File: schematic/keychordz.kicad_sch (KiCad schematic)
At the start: 40 parts, among them IC1 MCP73833-BZI_UN, J1 USB_C_Receptacle_USB2.0, J2 Conn_01x04_Male, SW1 SW_Push, SW2 SW_Push, SW3 SW_Push, SW4 SW_Push, SW5 SW_Push, SW6 SW_Push, SW7 SW_Push, SW9 SW_SPST, U1 nRF52840_Breakout

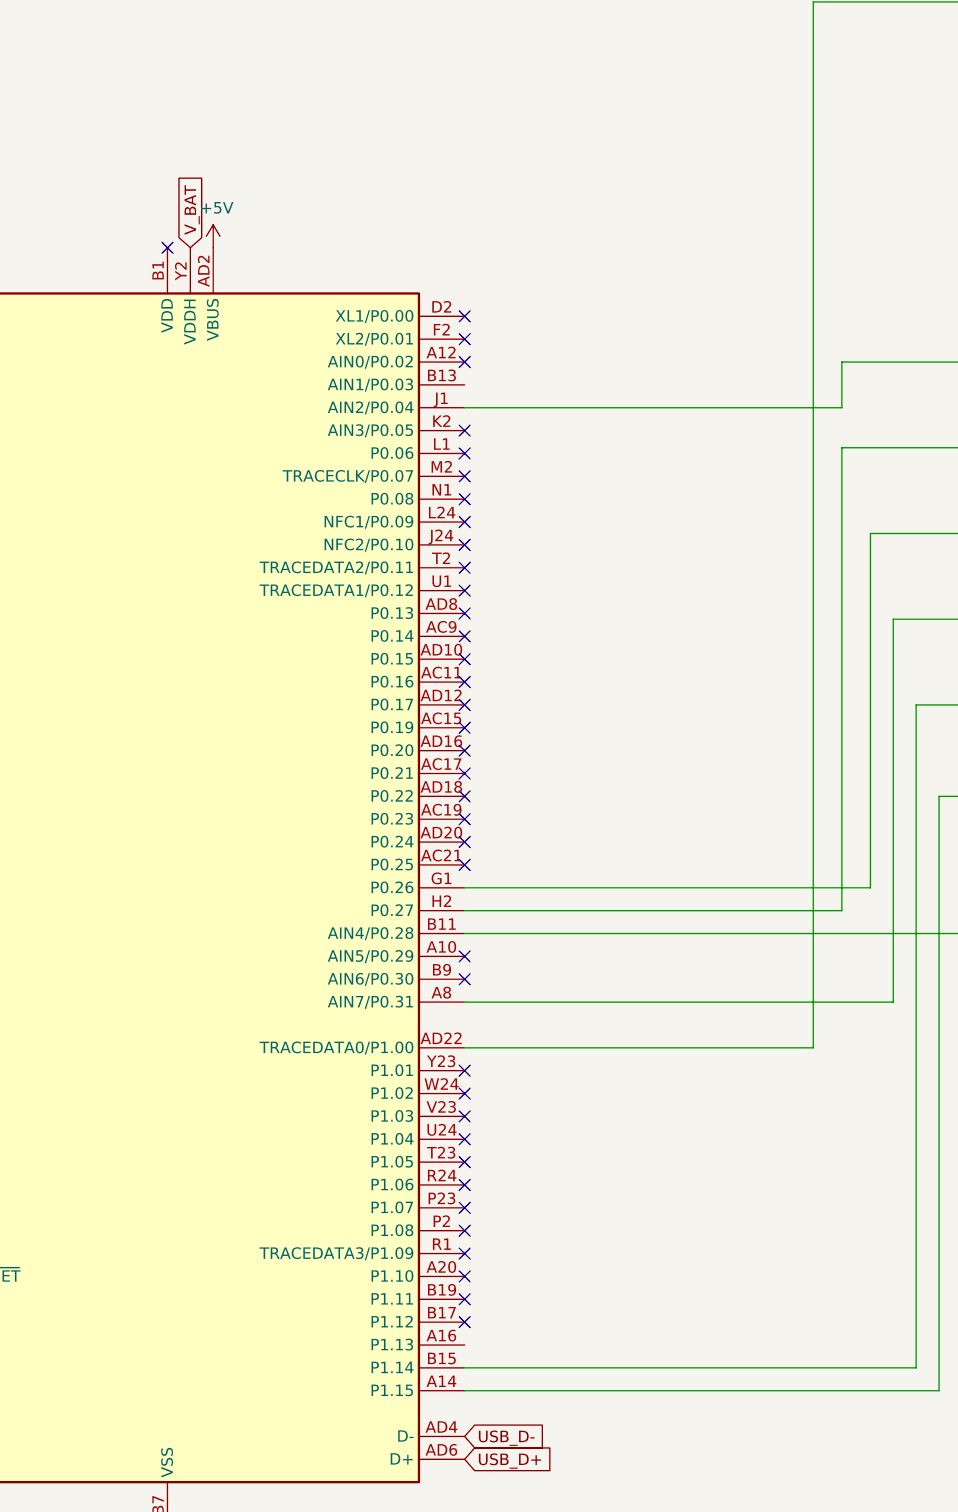
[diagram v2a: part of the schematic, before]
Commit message: update breakout without castellations
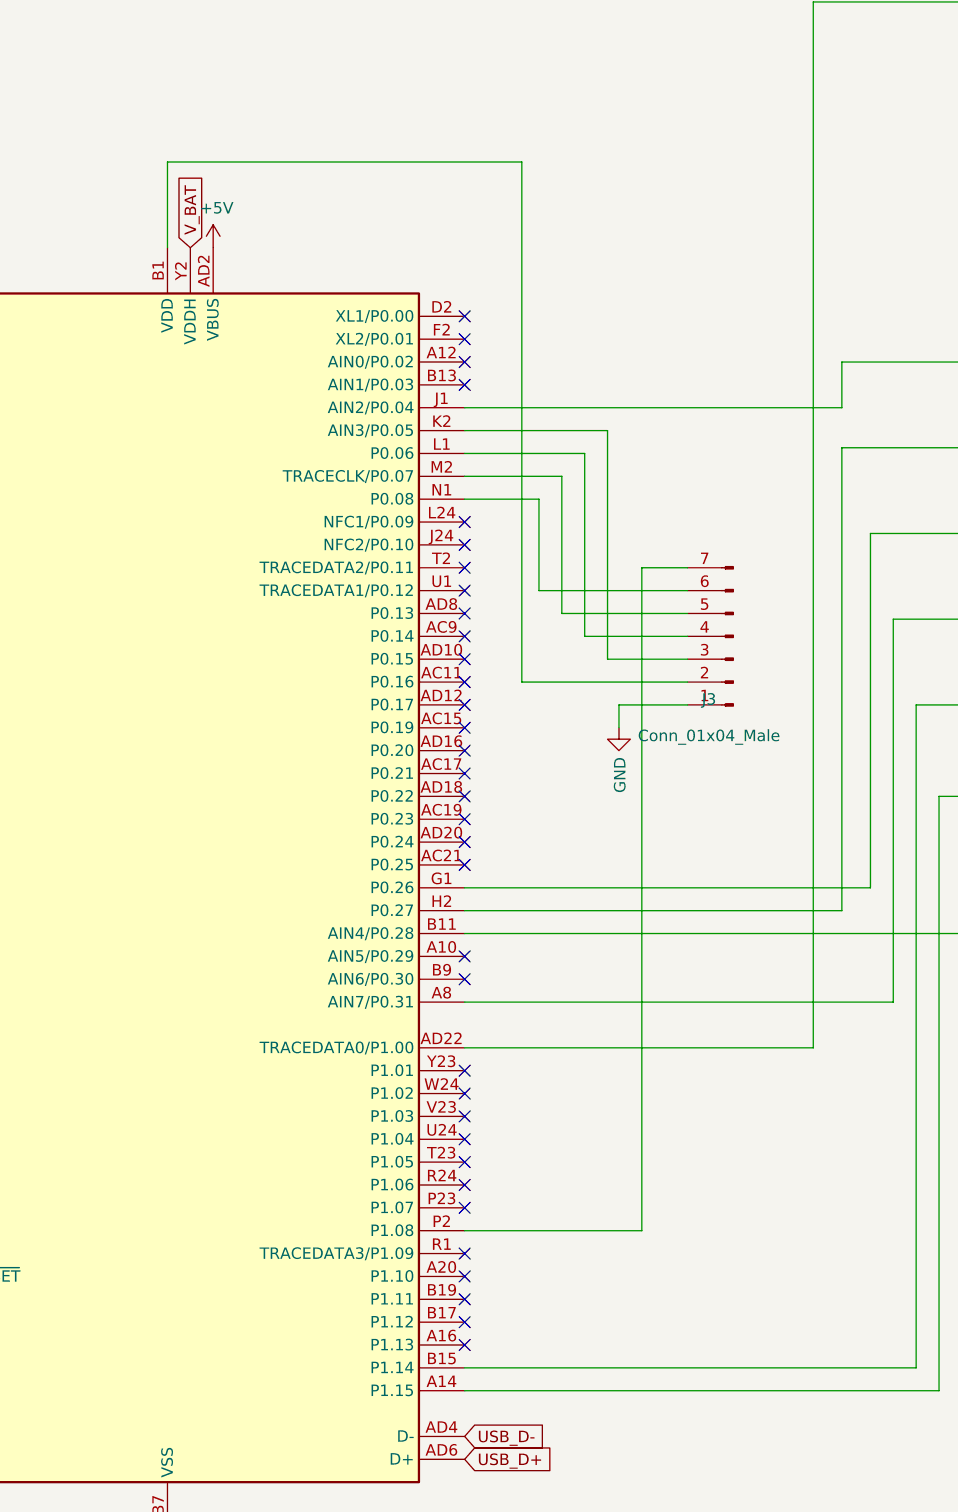
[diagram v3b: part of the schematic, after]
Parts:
- added J3: Conn_01x04_Male, Connector_PinHeader_2.54mm:PinHeader_1x07_P2.54mm_Vertical, symbol Connector:Conn_01x07_Male
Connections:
- net GND: now also J3.1 (Pin_1)
- net at U1.B1 (VDD): now also J3.2 (Pin_2)
- net at U1.K2 (AIN3/P0.05): now also J3.3 (Pin_3)
- net at U1.L1 (P0.06): now also J3.4 (Pin_4)
- net at U1.M2 (TRACECLK/P0.07): now also J3.5 (Pin_5)
- net at U1.N1 (P0.08): now also J3.6 (Pin_6)
- net at U1.P2 (P1.08): now also J3.7 (Pin_7)
- no-connect marks 41 -> 37
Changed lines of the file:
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@@
   (no_connect (at 46.355 53.34))
   (no_connect (at 46.355 55.88))
-  (no_connect (at 168.275 69.85))
   (no_connect (at 201.295 77.47))
   (no_connect (at 201.295 80.01))
   (no_connect (at 201.295 82.55))
-  (no_connect (at 201.295 90.17))
-  (no_connect (at 201.295 92.71))
-  (no_connect (at 201.295 95.25))
-  (no_connect (at 201.295 97.79))
+  (no_connect (at 201.295 85.09))
   (no_connect (at 201.295 100.33))
   (no_connect (at 201.295 102.87))
@@
   (no_connect (at 201.295 173.99))
   (no_connect (at 201.295 176.53))
-  (no_connect (at 201.295 179.07))
   (no_connect (at 201.295 181.61))
   (no_connect (at 201.295 184.15))
   (no_connect (at 201.295 186.69))
   (no_connect (at 201.295 189.23))
+  (no_connect (at 201.295 191.77))
   (wire (pts (xy 32.385 90.805) (xy 32.385 93.345))
     (stroke (width 0) (type solid) (color 0 0 0 0))
@@
     (stroke (width 0) (type solid) (color 0 0 0 0))
   )
+  (wire (pts (xy 168.275 60.325) (xy 207.645 60.325))
+    (stroke (width 0) (type solid) (color 0 0 0 0))
+  )
+  (wire (pts (xy 168.275 69.85) (xy 168.275 60.325))
+    (stroke (width 0) (type solid) (color 0 0 0 0))
+  )
   (wire (pts (xy 201.295 87.63) (xy 243.205 87.63))
     (stroke (width 0) (type solid) (color 0 0 0 0))
   )
+  (wire (pts (xy 201.295 90.17) (xy 217.17 90.17))
+    (stroke (width 0) (type solid) (color 0 0 0 0))
+  )
+  (wire (pts (xy 201.295 92.71) (xy 214.63 92.71))
+    (stroke (width 0) (type solid) (color 0 0 0 0))
+  )
+  (wire (pts (xy 201.295 95.25) (xy 212.09 95.25))
+    (stroke (width 0) (type solid) (color 0 0 0 0))
+  )
+  (wire (pts (xy 201.295 97.79) (xy 209.55 97.79))
+    (stroke (width 0) (type solid) (color 0 0 0 0))
+  )
   (wire (pts (xy 201.295 140.97) (xy 246.38 140.97))
     (stroke (width 0) (type solid) (color 0 0 0 0))
@@
     (stroke (width 0) (type solid) (color 0 0 0 0))
   )
+  (wire (pts (xy 201.295 179.07) (xy 220.98 179.07))
+    (stroke (width 0) (type solid) (color 0 0 0 0))
+  )
   (wire (pts (xy 201.295 194.31) (xy 251.46 194.31))
     (stroke (width 0) (type solid) (color 0 0 0 0))
   )
   (wire (pts (xy 201.295 196.85) (xy 254 196.85))
+    (stroke (width 0) (type solid) (color 0 0 0 0))
+  )
+  (wire (pts (xy 207.645 60.325) (xy 207.645 118.11))
+    (stroke (width 0) (type solid) (color 0 0 0 0))
+  )
+  (wire (pts (xy 207.645 118.11) (xy 226.06 118.11))
+    (stroke (width 0) (type solid) (color 0 0 0 0))
+  )
+  (wire (pts (xy 209.55 97.79) (xy 209.55 107.95))
+    (stroke (width 0) (type solid) (color 0 0 0 0))
+  )
+  (wire (pts (xy 209.55 107.95) (xy 226.06 107.95))
+    (stroke (width 0) (type solid) (color 0 0 0 0))
+  )
+  (wire (pts (xy 212.09 95.25) (xy 212.09 110.49))
+    (stroke (width 0) (type solid) (color 0 0 0 0))
+  )
+  (wire (pts (xy 212.09 110.49) (xy 226.06 110.49))
+    (stroke (width 0) (type solid) (color 0 0 0 0))
+  )
+  (wire (pts (xy 214.63 92.71) (xy 214.63 113.03))
+    (stroke (width 0) (type solid) (color 0 0 0 0))
+  )
+  (wire (pts (xy 214.63 113.03) (xy 226.06 113.03))
+    (stroke (width 0) (type solid) (color 0 0 0 0))
+  )
+  (wire (pts (xy 217.17 90.17) (xy 217.17 115.57))
+    (stroke (width 0) (type solid) (color 0 0 0 0))
+  )
+  (wire (pts (xy 217.17 115.57) (xy 226.06 115.57))
+    (stroke (width 0) (type solid) (color 0 0 0 0))
+  )
+  (wire (pts (xy 218.44 120.65) (xy 218.44 123.19))
+    (stroke (width 0) (type solid) (color 0 0 0 0))
+  )
+  (wire (pts (xy 220.98 105.41) (xy 226.06 105.41))
+    (stroke (width 0) (type solid) (color 0 0 0 0))
+  )
+  (wire (pts (xy 220.98 179.07) (xy 220.98 105.41))
+    (stroke (width 0) (type solid) (color 0 0 0 0))
+  )
+  (wire (pts (xy 226.06 120.65) (xy 218.44 120.65))
     (stroke (width 0) (type solid) (color 0 0 0 0))
   )
@@
     (pin "1")
   )
+  (symbol (lib_id "power:GND") (at 218.44 123.19 0) (unit 1)
+    (in_bom yes) (on_board yes)
+    (property "Reference" "#PWR0112" (id 0) (at 218.44 129.54 0)
+      (effects (font (size 1.27 1.27)) hide)
+    )
+    (property "Value" "GND" (id 1) (at 218.567 126.4412 90)
+      (effects (font (size 1.27 1.27)) (justify right))
+    )
+    (property "Footprint" "" (id 2) (at 218.44 123.19 0)
+      (effects (font (size 1.27 1.27)) hide)
+    )
+    (property "Datasheet" "" (id 3) (at 218.44 123.19 0)
+      (effects (font (size 1.27 1.27)) hide)
+    )
+    (pin "1")
+  )
   (symbol (lib_id "power:GND") (at 267.97 82.55 0) (unit 1)
     (in_bom yes) (on_board yes)
@@
     (pin "3")
     (pin "4")
+  )
+  (symbol (lib_id "Connector:Conn_01x07_Male") (at 231.14 113.03 180) (unit 1)
+    (in_bom yes) (on_board yes)
+    (property "Reference" "J3" (id 0) (at 228.4476 120.0342 0))
+    (property "Value" "Conn_01x04_Male" (id 1) (at 228.4476 124.0855 0))
+    (property "Footprint" "Connector_PinHeader_2.54mm:PinHeader_1x07_P2.54mm_Vertical" (id 2) (at 231.14 113.03 0)
+      (effects (font (size 1.27 1.27)) hide)
+    )
+    (property "Datasheet" "~" (id 3) (at 231.14 113.03 0)
+      (effects (font (size 1.27 1.27)) hide)
+    )
+    (pin "1")
+    (pin "2")
+    (pin "3")
+    (pin "4")
+    (pin "5")
+    (pin "6")
+    (pin "7")
   )
   (symbol (lib_id "LED:WS2812B") (at 302.895 73.66 90) (unit 1)
@@
       (reference "#PWR0111") (unit 1) (value "+5V") (footprint "")
     )
+    (path "/ff193ba5-4bef-4430-b15f-592f6a81f044"
+      (reference "#PWR0112") (unit 1) (value "GND") (footprint "")
+    )
     (path "/00000000-0000-0000-0000-000060329735"
       (reference "BT1") (unit 1) (value "Battery_Cell") (footprint "Battery:BatteryHolder_MPD_BH-18650-PC2")
@@
       (reference "J2") (unit 1) (value "Conn_01x04_Male") (footprint "Connector_PinHeader_2.54mm:PinHeader_1x04_P2.54mm_Vertical")
     )
+    (path "/3cb004f3-895d-4ebf-a616-a223fca20acb"
+      (reference "J3") (unit 1) (value "Conn_01x04_Male") (footprint "Connector_PinHeader_2.54mm:PinHeader_1x07_P2.54mm_Vertical")
+    )
     (path "/00000000-0000-0000-0000-0000603424c4"
